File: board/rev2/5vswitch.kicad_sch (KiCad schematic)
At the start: 15 parts, among them Q1 WSD40120DN56G, U3 TPS259472ARPWR, U4 LM5050-1

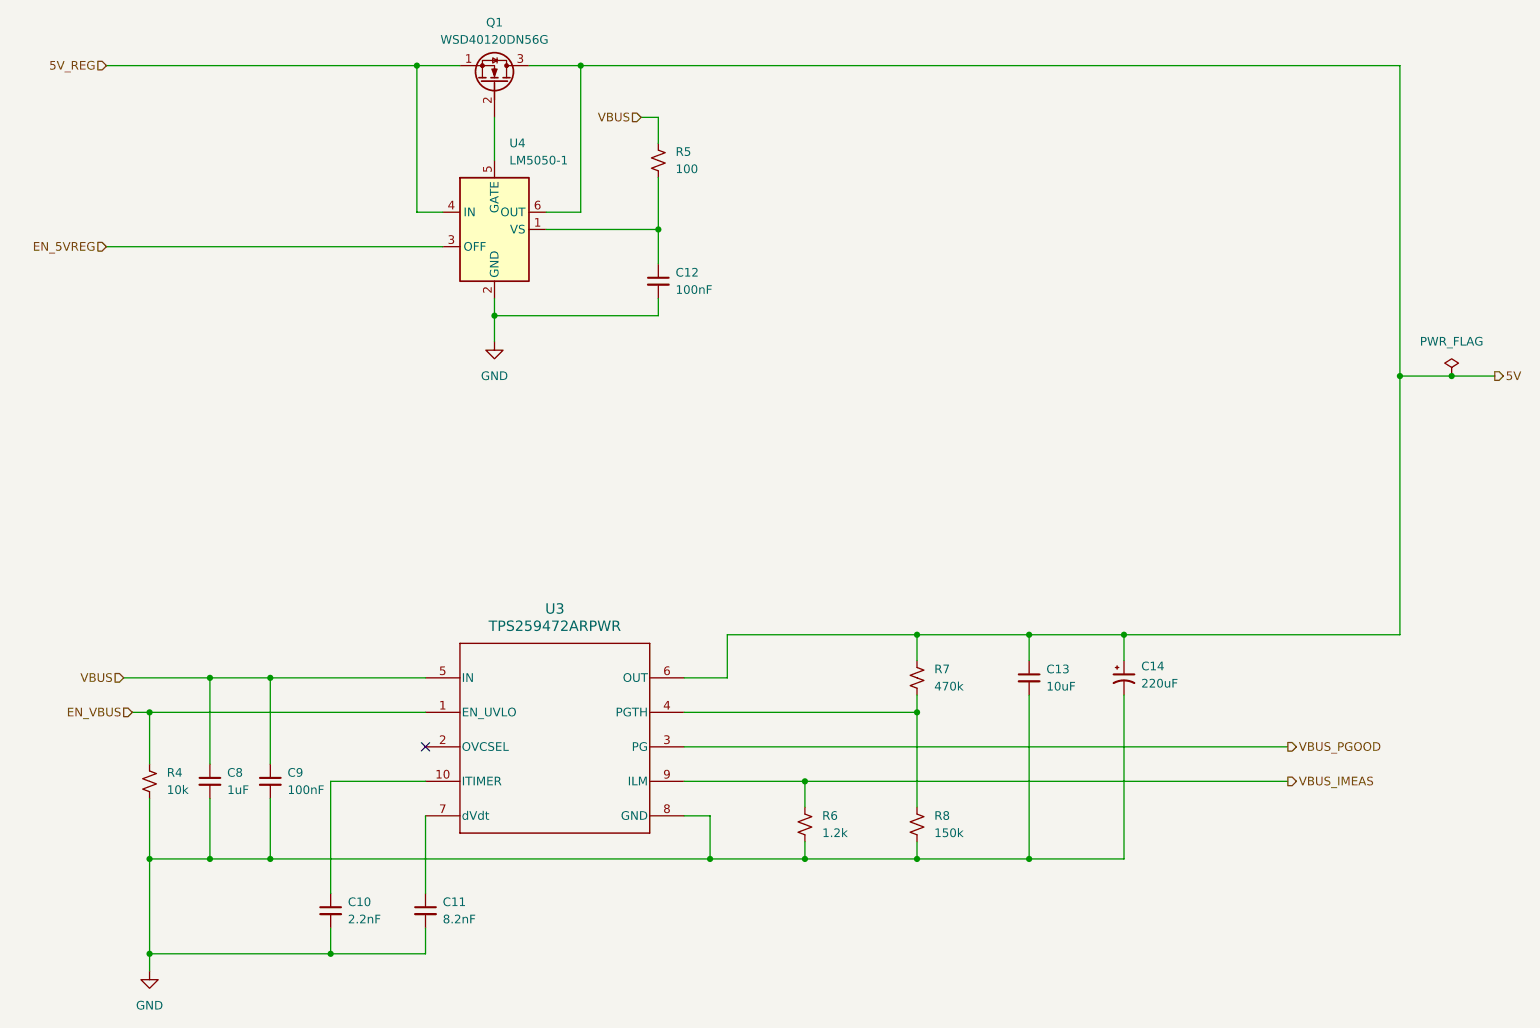
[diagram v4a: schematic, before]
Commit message: Really finish rev2 board schematic
- fix some more footprints
  - move to real SD card holder, for example
- repair part numbers
- add LCSC part refs to everything
- add even more caps to the 3.3V reg output
  - really should use an LDO but meh it should be fine

total BOM cost for 5 of them is apparently 160 CAD, or like 32 dollars
each (don't think that includes the feeder fees tho)
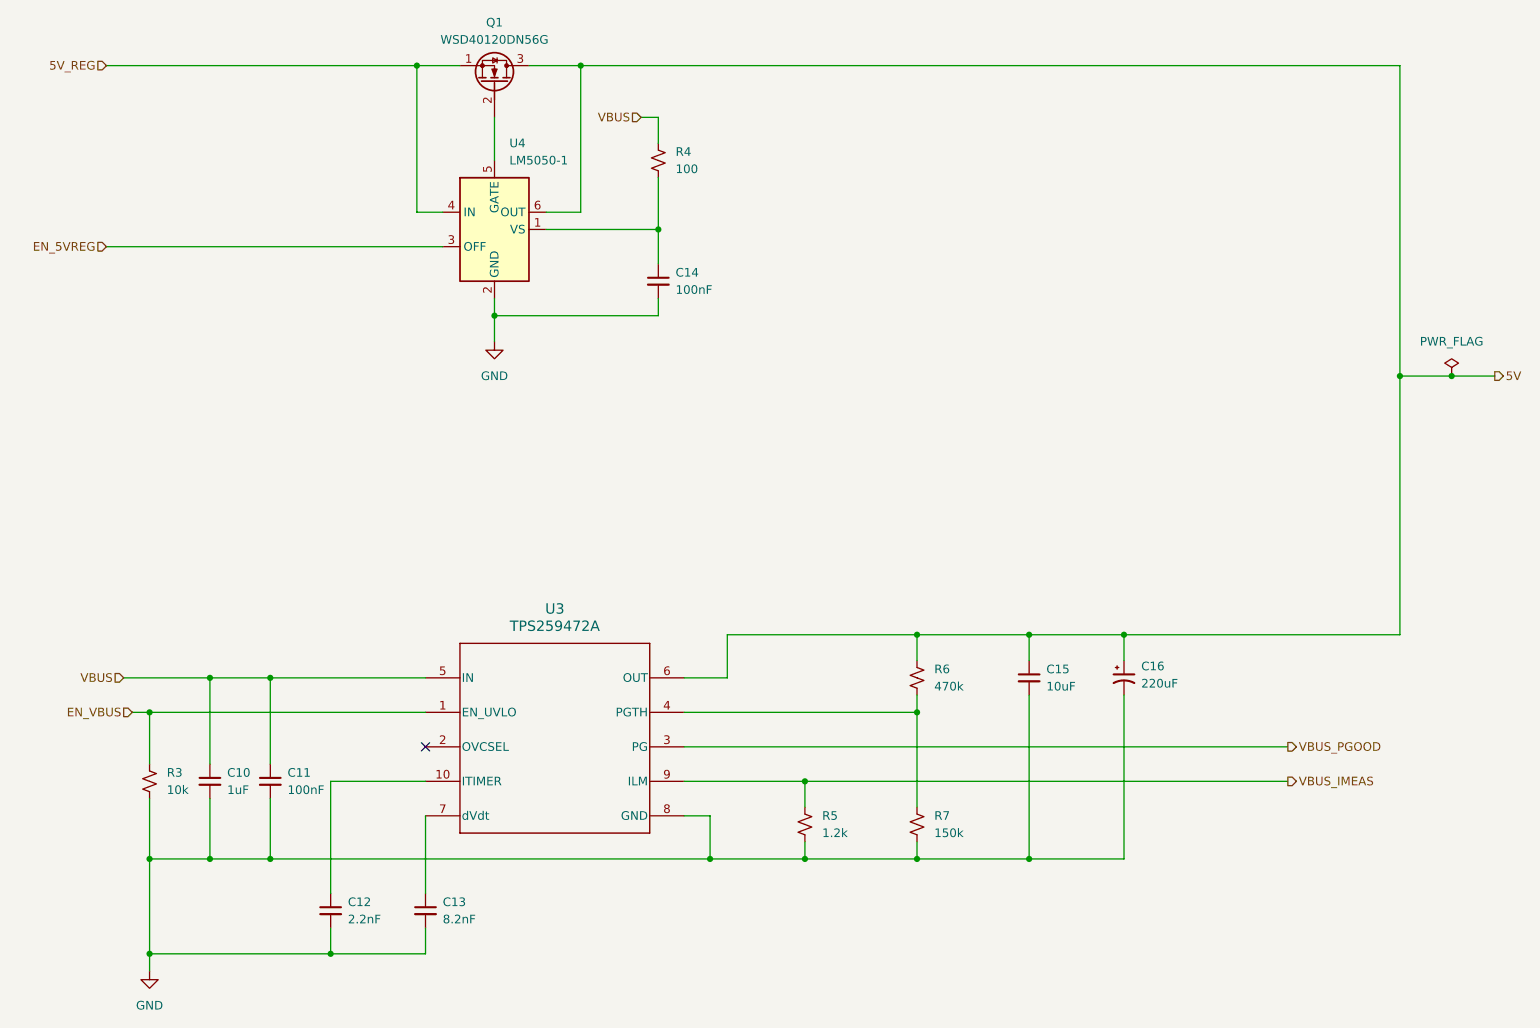
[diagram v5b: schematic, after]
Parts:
- C10: renamed from C8; LCSC (none) -> C15849
- C11: renamed from C9; LCSC (none) -> C307331
- C12: renamed from C10; LCSC (none) -> C1604
- C13: renamed from C11; LCSC (none) -> C1322360
- C14: renamed from C12; LCSC (none) -> C307331
- C15: renamed from C13; LCSC (none) -> C13585
- C16: renamed from C14; LCSC (none) -> C106697
- Q1: LCSC (none) -> C507088
- R3: renamed from R4; LCSC (none) -> C17414
- R4: renamed from R5; LCSC (none) -> C17901
- R5: renamed from R6; LCSC (none) -> C17379
- R6: renamed from R7; LCSC (none) -> C17709
- R7: renamed from R8; LCSC (none) -> C17470
- U3: value TPS259472ARPWR -> TPS259472A; LCSC (none) -> C3662789
- U4: LCSC (none) -> C473393; Part LM5050-1 -> LM5050MKX-1/NOPB
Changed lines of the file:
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@@
 		(dnp no)
 		(fields_autoplaced yes)
-		(property "Reference" "C14"
+		(property "Reference" "C16"
 			(at 182.88 113.8681 0)
 			(effects
@@
 			)
 		)
+		(property "LCSC" "C106697"
+			(at 180.34 115.57 0)
+			(effects
+				(font
+					(size 1.27 1.27)
+				)
+				(hide yes)
+			)
+		)
 		(pin "1"
 		)
@@
 			(project "mainboard"
 				(path "/32eb05c7-b4a6-42f3-8fb3-43453631100f/802d77e5-f72d-443e-abfe-d20b44acef6c/65e76cbc-a8ae-47e0-859c-8ff07b1a8d6c"
-					(reference "C14")
+					(reference "C16")
 					(unit 1)
 				)
@@
 		(dnp no)
 		(fields_autoplaced yes)
-		(property "Reference" "C13"
+		(property "Reference" "C15"
 			(at 168.91 114.3062 0)
 			(effects
@@
 			)
 		)
+		(property "LCSC" "C13585"
+			(at 166.37 115.57 0)
+			(effects
+				(font
+					(size 1.27 1.27)
+				)
+				(hide yes)
+			)
+		)
 		(pin "2"
 		)
@@
 			(project "mainboard"
 				(path "/32eb05c7-b4a6-42f3-8fb3-43453631100f/802d77e5-f72d-443e-abfe-d20b44acef6c/65e76cbc-a8ae-47e0-859c-8ff07b1a8d6c"
-					(reference "C13")
+					(reference "C15")
 					(unit 1)
 				)
@@
 		(dnp no)
 		(fields_autoplaced yes)
-		(property "Reference" "C12"
+		(property "Reference" "C14"
 			(at 114.3 55.8862 0)
 			(effects
@@
 			)
 		)
+		(property "LCSC" "C307331 "
+			(at 111.76 57.15 0)
+			(effects
+				(font
+					(size 1.27 1.27)
+				)
+				(hide yes)
+			)
+		)
 		(pin "1"
 		)
@@
 			(project ""
 				(path "/32eb05c7-b4a6-42f3-8fb3-43453631100f/802d77e5-f72d-443e-abfe-d20b44acef6c/65e76cbc-a8ae-47e0-859c-8ff07b1a8d6c"
-					(reference "C12")
+					(reference "C14")
 					(unit 1)
 				)
@@
 			)
 		)
-		(property "Part" "LM5050-1"
+		(property "Part" "LM5050MKX-1/NOPB"
+			(at 87.63 49.53 0)
+			(effects
+				(font
+					(size 1.27 1.27)
+				)
+				(hide yes)
+			)
+		)
+		(property "LCSC" "C473393"
 			(at 87.63 49.53 0)
 			(effects
@@
 		(dnp no)
 		(fields_autoplaced yes)
-		(property "Reference" "R6"
+		(property "Reference" "R5"
 			(at 135.89 135.8899 0)
 			(effects
@@
 			)
 		)
+		(property "LCSC" "C17379"
+			(at 133.35 137.16 0)
+			(effects
+				(font
+					(size 1.27 1.27)
+				)
+				(hide yes)
+			)
+		)
 		(pin "2"
 		)
@@
 			(project "mainboard"
 				(path "/32eb05c7-b4a6-42f3-8fb3-43453631100f/802d77e5-f72d-443e-abfe-d20b44acef6c/65e76cbc-a8ae-47e0-859c-8ff07b1a8d6c"
-					(reference "R6")
+					(reference "R5")
 					(unit 1)
 				)
@@
 		(dnp no)
 		(fields_autoplaced yes)
-		(property "Reference" "R4"
+		(property "Reference" "R3"
 			(at 39.37 129.5399 0)
 			(effects
@@
 			)
 		)
+		(property "LCSC" "C17414 "
+			(at 36.83 130.81 0)
+			(effects
+				(font
+					(size 1.27 1.27)
+				)
+				(hide yes)
+			)
+		)
 		(pin "1"
 		)
@@
 			(project "mainboard"
 				(path "/32eb05c7-b4a6-42f3-8fb3-43453631100f/802d77e5-f72d-443e-abfe-d20b44acef6c/65e76cbc-a8ae-47e0-859c-8ff07b1a8d6c"
-					(reference "R4")
+					(reference "R3")
 					(unit 1)
 				)
@@
 		(dnp no)
 		(fields_autoplaced yes)
-		(property "Reference" "R5"
+		(property "Reference" "R4"
 			(at 114.3 38.0999 0)
 			(effects
@@
 			)
 		)
+		(property "LCSC" "C17901"
+			(at 111.76 39.37 0)
+			(effects
+				(font
+					(size 1.27 1.27)
+				)
+				(hide yes)
+			)
+		)
 		(pin "2"
 		)
@@
 			(project "mainboard"
 				(path "/32eb05c7-b4a6-42f3-8fb3-43453631100f/802d77e5-f72d-443e-abfe-d20b44acef6c/65e76cbc-a8ae-47e0-859c-8ff07b1a8d6c"
-					(reference "R5")
+					(reference "R4")
 					(unit 1)
 				)
@@
 			)
 		)
-		(property "Value" "TPS259472ARPWR"
+		(property "Value" "TPS259472A"
 			(at 96.52 107.95 0)
 			(effects
@@
 			)
 		)
+		(property "LCSC" "C3662789"
+			(at 77.47 115.57 0)
+			(effects
+				(font
+					(size 1.27 1.27)
+				)
+				(hide yes)
+			)
+		)
 		(pin "9"
 		)
@@
 		(dnp no)
 		(fields_autoplaced yes)
-		(property "Reference" "C8"
+		(property "Reference" "C10"
 			(at 48.26 129.5462 0)
 			(effects
@@
 			)
 		)
+		(property "LCSC" "C15849"
+			(at 45.72 130.81 0)
+			(effects
+				(font
+					(size 1.27 1.27)
+				)
+				(hide yes)
+			)
+		)
 		(pin "1"
 		)
@@
 			(project "mainboard"
 				(path "/32eb05c7-b4a6-42f3-8fb3-43453631100f/802d77e5-f72d-443e-abfe-d20b44acef6c/65e76cbc-a8ae-47e0-859c-8ff07b1a8d6c"
-					(reference "C8")
+					(reference "C10")
 					(unit 1)
 				)
@@
 		(dnp no)
 		(fields_autoplaced yes)
-		(property "Reference" "#FLG01"
+		(property "Reference" "#FLG04"
 			(at 228.6 69.215 0)
 			(effects
@@
 			(project ""
 				(path "/32eb05c7-b4a6-42f3-8fb3-43453631100f/802d77e5-f72d-443e-abfe-d20b44acef6c/65e76cbc-a8ae-47e0-859c-8ff07b1a8d6c"
-					(reference "#FLG01")
+					(reference "#FLG04")
 					(unit 1)
 				)
@@
 		(dnp no)
 		(fields_autoplaced yes)
-		(property "Reference" "C9"
+		(property "Reference" "C11"
 			(at 57.15 129.5462 0)
 			(effects
@@
 			)
 		)
+		(property "LCSC" "C307331 "
+			(at 54.61 130.81 0)
+			(effects
+				(font
+					(size 1.27 1.27)
+				)
+				(hide yes)
+			)
+		)
 		(pin "2"
 		)
@@
 			(project "mainboard"
 				(path "/32eb05c7-b4a6-42f3-8fb3-43453631100f/802d77e5-f72d-443e-abfe-d20b44acef6c/65e76cbc-a8ae-47e0-859c-8ff07b1a8d6c"
-					(reference "C9")
+					(reference "C11")
 					(unit 1)
 				)
@@
 		(dnp no)
 		(fields_autoplaced yes)
-		(property "Reference" "C11"
+		(property "Reference" "C13"
 			(at 80.01 148.5962 0)
 			(effects
@@
 			)
 		)
+		(property "LCSC" "C1322360"
+			(at 77.47 149.86 0)
+			(effects
+				(font
+					(size 1.27 1.27)
+				)
+				(hide yes)
+			)
+		)
 		(pin "1"
 		)
@@
 			(project "mainboard"
 				(path "/32eb05c7-b4a6-42f3-8fb3-43453631100f/802d77e5-f72d-443e-abfe-d20b44acef6c/65e76cbc-a8ae-47e0-859c-8ff07b1a8d6c"
-					(reference "C11")
+					(reference "C13")
 					(unit 1)
 				)
@@
 		(dnp no)
 		(fields_autoplaced yes)
-		(property "Reference" "C10"
+		(property "Reference" "C12"
 			(at 66.04 148.5962 0)
 			(effects
@@
 			)
 		)
+		(property "LCSC" "C1604"
+			(at 63.5 149.86 0)
+			(effects
+				(font
+					(size 1.27 1.27)
+				)
+				(hide yes)
+			)
+		)
 		(pin "1"
 		)
@@
 			(project "mainboard"
 				(path "/32eb05c7-b4a6-42f3-8fb3-43453631100f/802d77e5-f72d-443e-abfe-d20b44acef6c/65e76cbc-a8ae-47e0-859c-8ff07b1a8d6c"
-					(reference "C10")
+					(reference "C12")
 					(unit 1)
 				)
@@
 			)
 		)
+		(property "LCSC" "C507088"
+			(at 87.63 27.94 90)
+			(effects
+				(font
+					(size 1.27 1.27)
+				)
+				(hide yes)
+			)
+		)
 		(pin "1"
 		)
@@
 		(dnp no)
 		(fields_autoplaced yes)
-		(property "Reference" "R8"
+		(property "Reference" "R7"
 			(at 152.4 135.8899 0)
 			(effects
@@
 			)
 		)
+		(property "LCSC" "C17470"
+			(at 149.86 137.16 0)
+			(effects
+				(font
+					(size 1.27 1.27)
+				)
+				(hide yes)
+			)
+		)
 		(pin "2"
 		)
@@
 			(project "mainboard"
 				(path "/32eb05c7-b4a6-42f3-8fb3-43453631100f/802d77e5-f72d-443e-abfe-d20b44acef6c/65e76cbc-a8ae-47e0-859c-8ff07b1a8d6c"
-					(reference "R8")
+					(reference "R7")
 					(unit 1)
 				)
@@
 		(dnp no)
 		(fields_autoplaced yes)
-		(property "Reference" "R7"
+		(property "Reference" "R6"
 			(at 152.4 114.2999 0)
 			(effects
@@
 			)
 		)
+		(property "LCSC" "C17709"
+			(at 149.86 115.57 0)
+			(effects
+				(font
+					(size 1.27 1.27)
+				)
+				(hide yes)
+			)
+		)
 		(pin "2"
 		)
@@
 			(project "mainboard"
 				(path "/32eb05c7-b4a6-42f3-8fb3-43453631100f/802d77e5-f72d-443e-abfe-d20b44acef6c/65e76cbc-a8ae-47e0-859c-8ff07b1a8d6c"
-					(reference "R7")
-					(unit 1)
-				)
+					(reference "R6")
+					(unit 1)
+				)

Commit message: Start board
add a few extra bypass caps too, and swap some pins on the USB mux

i forgot to add a bypass cap on the tpd6s so that also needs to happen

truly 63 capacitors is not enough
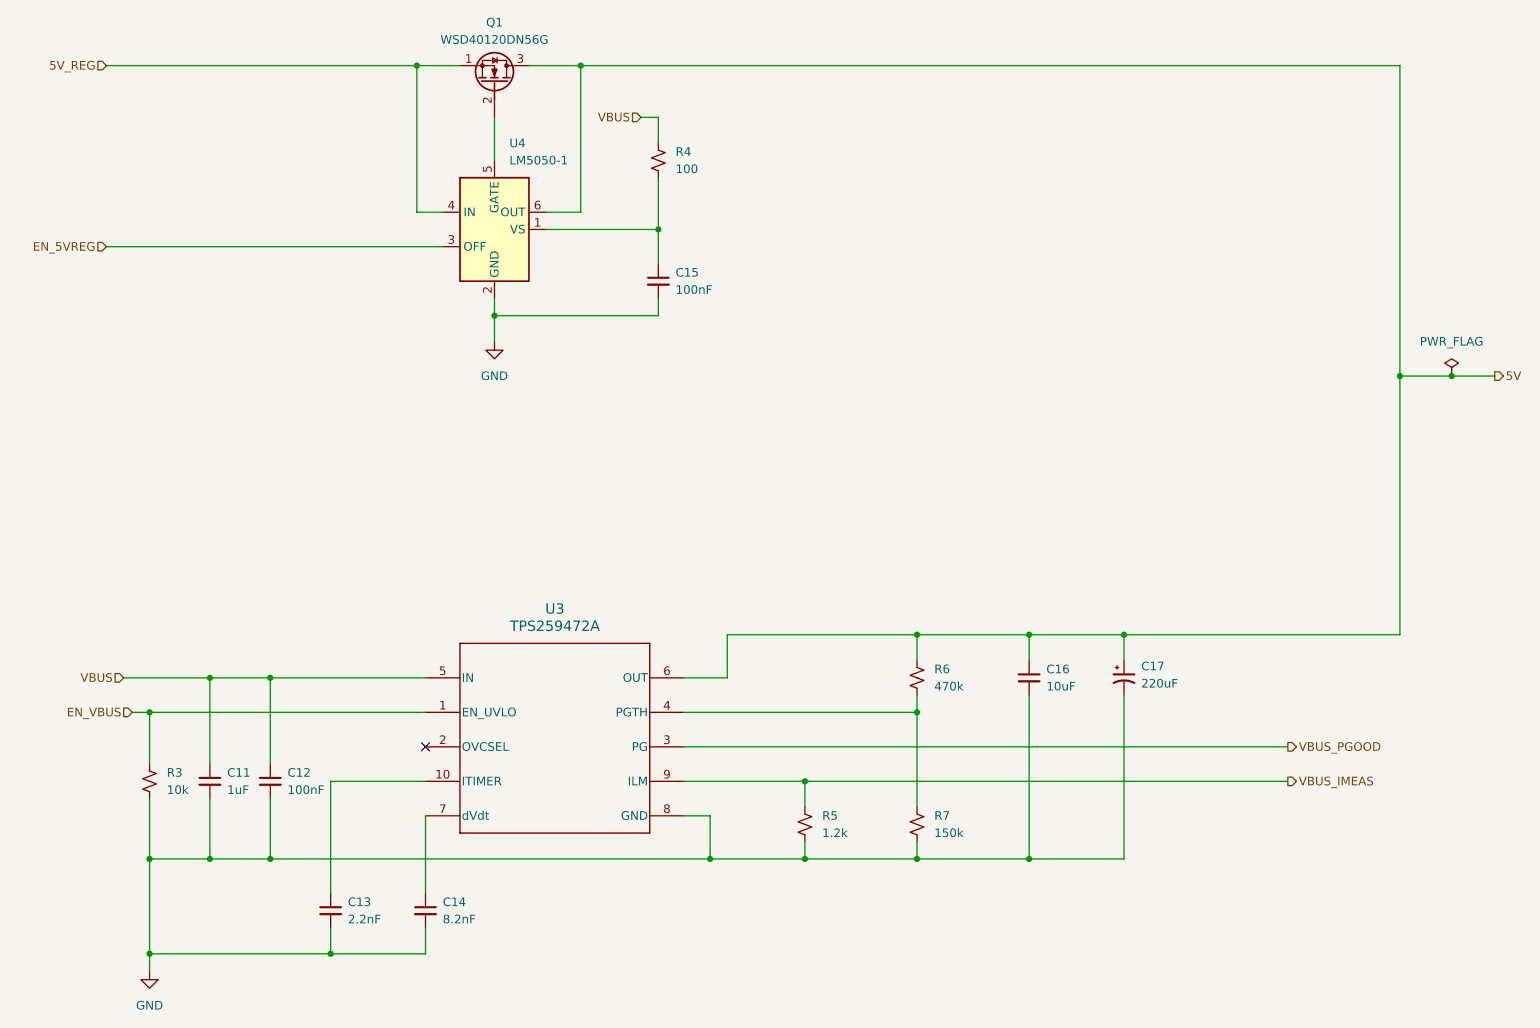
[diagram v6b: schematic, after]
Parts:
- renumbered C10 to C11, C11 to C12, C12 to C13, C13 to C14, C14 to C15, C15 to C16, C16 to C17
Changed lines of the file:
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@@
 		(dnp no)
 		(fields_autoplaced yes)
-		(property "Reference" "C16"
+		(property "Reference" "C17"
 			(at 182.88 113.8681 0)
 			(effects
@@
 			(project "mainboard"
 				(path "/32eb05c7-b4a6-42f3-8fb3-43453631100f/802d77e5-f72d-443e-abfe-d20b44acef6c/65e76cbc-a8ae-47e0-859c-8ff07b1a8d6c"
-					(reference "C16")
+					(reference "C17")
 					(unit 1)
 				)
@@
 		(dnp no)
 		(fields_autoplaced yes)
-		(property "Reference" "C15"
+		(property "Reference" "C16"
 			(at 168.91 114.3062 0)
 			(effects
@@
 			(project "mainboard"
 				(path "/32eb05c7-b4a6-42f3-8fb3-43453631100f/802d77e5-f72d-443e-abfe-d20b44acef6c/65e76cbc-a8ae-47e0-859c-8ff07b1a8d6c"
-					(reference "C15")
+					(reference "C16")
 					(unit 1)
 				)
@@
 		(dnp no)
 		(fields_autoplaced yes)
-		(property "Reference" "C14"
+		(property "Reference" "C15"
 			(at 114.3 55.8862 0)
 			(effects
@@
 			(project ""
 				(path "/32eb05c7-b4a6-42f3-8fb3-43453631100f/802d77e5-f72d-443e-abfe-d20b44acef6c/65e76cbc-a8ae-47e0-859c-8ff07b1a8d6c"
-					(reference "C14")
+					(reference "C15")
 					(unit 1)
 				)
@@
 		(dnp no)
 		(fields_autoplaced yes)
-		(property "Reference" "C10"
+		(property "Reference" "C11"
 			(at 48.26 129.5462 0)
 			(effects
@@
 			(project "mainboard"
 				(path "/32eb05c7-b4a6-42f3-8fb3-43453631100f/802d77e5-f72d-443e-abfe-d20b44acef6c/65e76cbc-a8ae-47e0-859c-8ff07b1a8d6c"
-					(reference "C10")
+					(reference "C11")
 					(unit 1)
 				)
@@
 		(dnp no)
 		(fields_autoplaced yes)
-		(property "Reference" "C11"
+		(property "Reference" "C12"
 			(at 57.15 129.5462 0)
 			(effects
@@
 			(project "mainboard"
 				(path "/32eb05c7-b4a6-42f3-8fb3-43453631100f/802d77e5-f72d-443e-abfe-d20b44acef6c/65e76cbc-a8ae-47e0-859c-8ff07b1a8d6c"
-					(reference "C11")
+					(reference "C12")
 					(unit 1)
 				)
@@
 		(dnp no)
 		(fields_autoplaced yes)
-		(property "Reference" "C13"
+		(property "Reference" "C14"
 			(at 80.01 148.5962 0)
 			(effects
@@
 			(project "mainboard"
 				(path "/32eb05c7-b4a6-42f3-8fb3-43453631100f/802d77e5-f72d-443e-abfe-d20b44acef6c/65e76cbc-a8ae-47e0-859c-8ff07b1a8d6c"
-					(reference "C13")
+					(reference "C14")
 					(unit 1)
 				)
@@
 		(dnp no)
 		(fields_autoplaced yes)
-		(property "Reference" "C12"
+		(property "Reference" "C13"
 			(at 66.04 148.5962 0)
 			(effects
@@
 			(project "mainboard"
 				(path "/32eb05c7-b4a6-42f3-8fb3-43453631100f/802d77e5-f72d-443e-abfe-d20b44acef6c/65e76cbc-a8ae-47e0-859c-8ff07b1a8d6c"
-					(reference "C12")
-					(unit 1)
-				)
+					(reference "C13")
+					(unit 1)
+				)

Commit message: More tweaks to schematic, start laying out regulators
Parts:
- R3: footprint Resistor_SMD:R_0805_2012Metric -> Resistor_SMD:R_0402_1005Metric; LCSC C17414 -> C25744; Part 0805W8F1002T5E -> 0402WGF1002TCE
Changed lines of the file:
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@@
 			)
 		)
-		(property "Footprint" "Resistor_SMD:R_0805_2012Metric"
+		(property "Footprint" "Resistor_SMD:R_0402_1005Metric"
 			(at 36.83 130.81 0)
 			(effects
@@
 			)
 		)
-		(property "Part" "0805W8F1002T5E"
+		(property "Part" "0402WGF1002TCE"
 			(at 36.83 130.81 0)
 			(effects
@@
 			)
 		)
-		(property "LCSC" "C17414 "
+		(property "LCSC" "C25744"
 			(at 36.83 130.81 0)
 			(effects

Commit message: Finish board rev2
woo another pcb
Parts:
- C16: footprint Capacitor_SMD:C_1210_3225Metric -> Capacitor_SMD:C_1206_3216Metric
